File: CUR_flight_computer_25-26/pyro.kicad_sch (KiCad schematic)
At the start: 22 parts, among them J10 TB0011-350-02GR, J11 TB0011-350-02GR, J8 TB0011-350-02GR, J9 TB0011-350-02GR, U12 BUK9K25-40RAX, U13 BUK9K25-40RAX

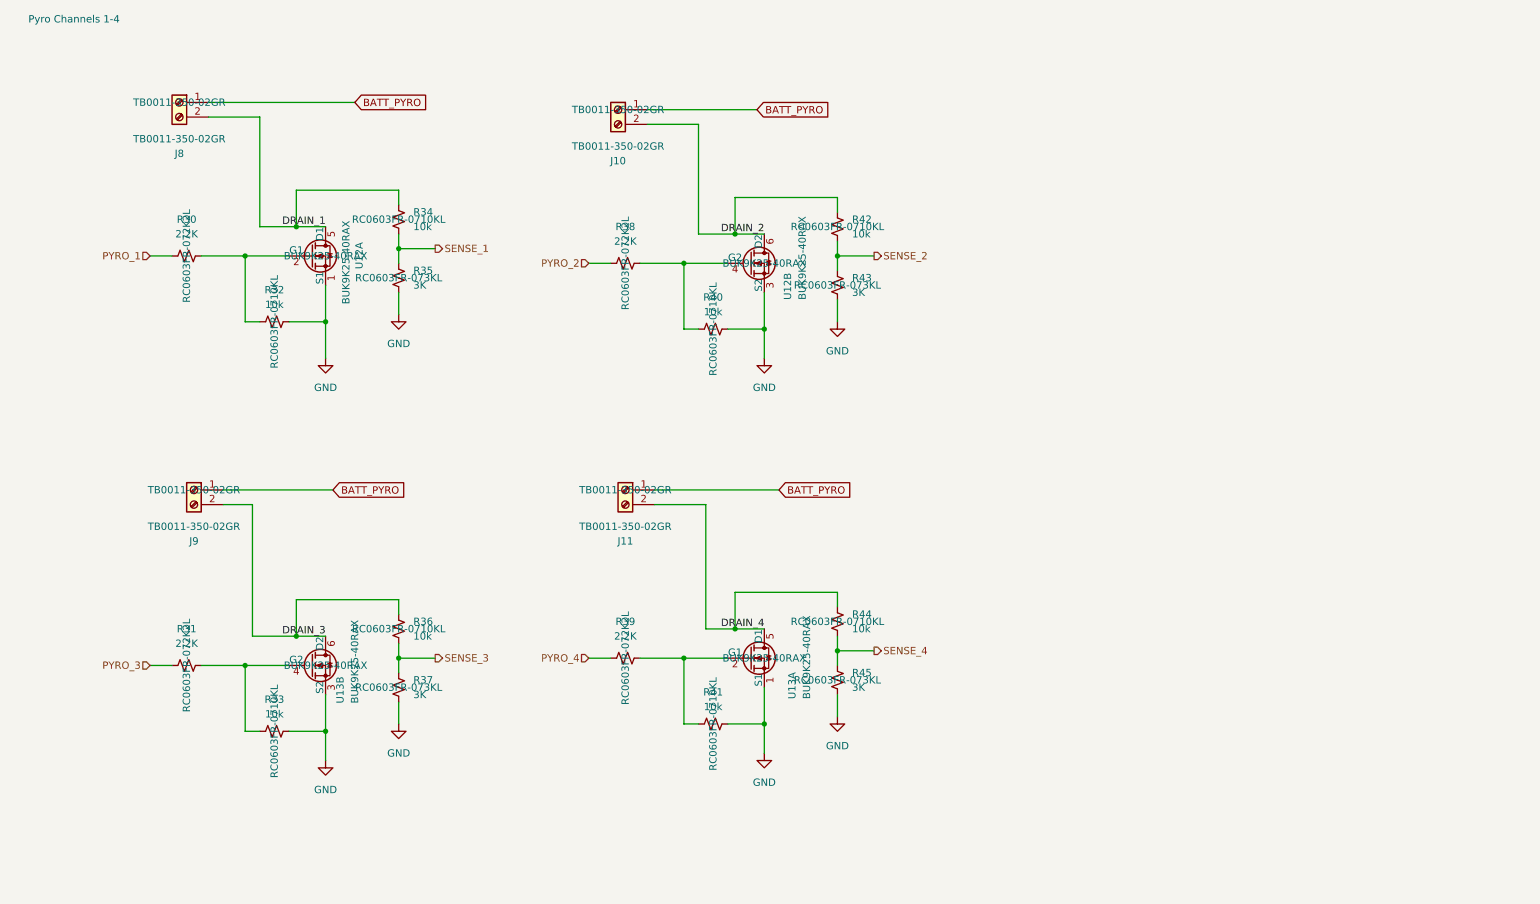
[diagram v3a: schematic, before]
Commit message: Hide MPNs
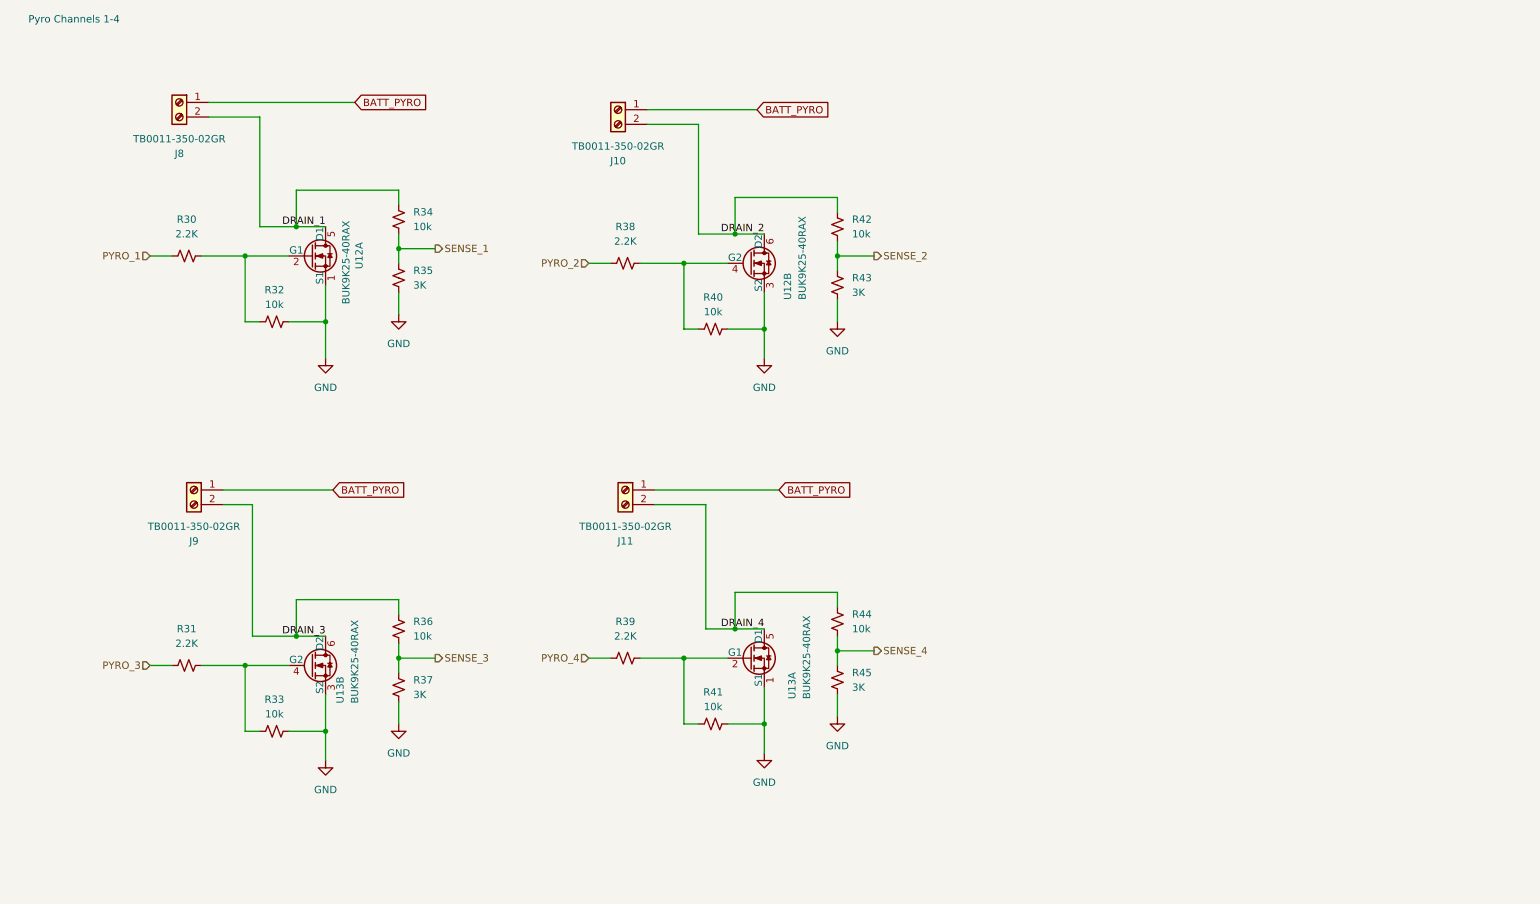
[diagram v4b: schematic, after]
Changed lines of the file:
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@@
 					(size 1.27 1.27)
 				)
+				(hide yes)
 			)
 		)
@@
 					(size 1.27 1.27)
 				)
+				(hide yes)
 			)
 		)
@@
 					(size 1.27 1.27)
 				)
+				(hide yes)
 			)
 		)
@@
 					(size 1.27 1.27)
 				)
+				(hide yes)
 			)
 		)
@@
 					(size 1.27 1.27)
 				)
+				(hide yes)
 			)
 		)
@@
 					(size 1.27 1.27)
 				)
+				(hide yes)
 			)
 		)
@@
 					(size 1.27 1.27)
 				)
+				(hide yes)
 			)
 		)
@@
 					(size 1.27 1.27)
 				)
+				(hide yes)
 			)
 		)
@@
 					(size 1.27 1.27)
 				)
+				(hide yes)
 			)
 		)
@@
 					(size 1.27 1.27)
 				)
+				(hide yes)
 			)
 		)
@@
 					(size 1.27 1.27)
 				)
+				(hide yes)
 			)
 		)
@@
 					(size 1.27 1.27)
 				)
+				(hide yes)
 			)
 		)
@@
 					(size 1.27 1.27)
 				)
+				(hide yes)
 			)
 		)
@@
 					(size 1.27 1.27)
 				)
+				(hide yes)
 			)
 		)
@@
 					(size 1.27 1.27)
 				)
+				(hide yes)
 			)
 		)
@@
 					(size 1.27 1.27)
 				)
+				(hide yes)
 			)
 		)
@@
 					(size 1.27 1.27)
 				)
+				(hide yes)
 			)
 		)
@@
 					(size 1.27 1.27)
 				)
+				(hide yes)
 			)
 		)
@@
 					(size 1.27 1.27)
 				)
+				(hide yes)
 			)
 		)
@@
 					(size 1.27 1.27)
 				)
+				(hide yes)
 			)
 		)
@@
 					(size 1.27 1.27)
 				)
+				(hide yes)
 			)
 		)
@@
 					(size 1.27 1.27)
 				)
+				(hide yes)
 			)
 		)
@@
 					(size 1.27 1.27)
 				)
+				(hide yes)
 			)
 		)
@@
 					(size 1.27 1.27)
 				)
-			)
-		)
+				(hide yes)
+			)
+		)

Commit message: Cleaned up schematic
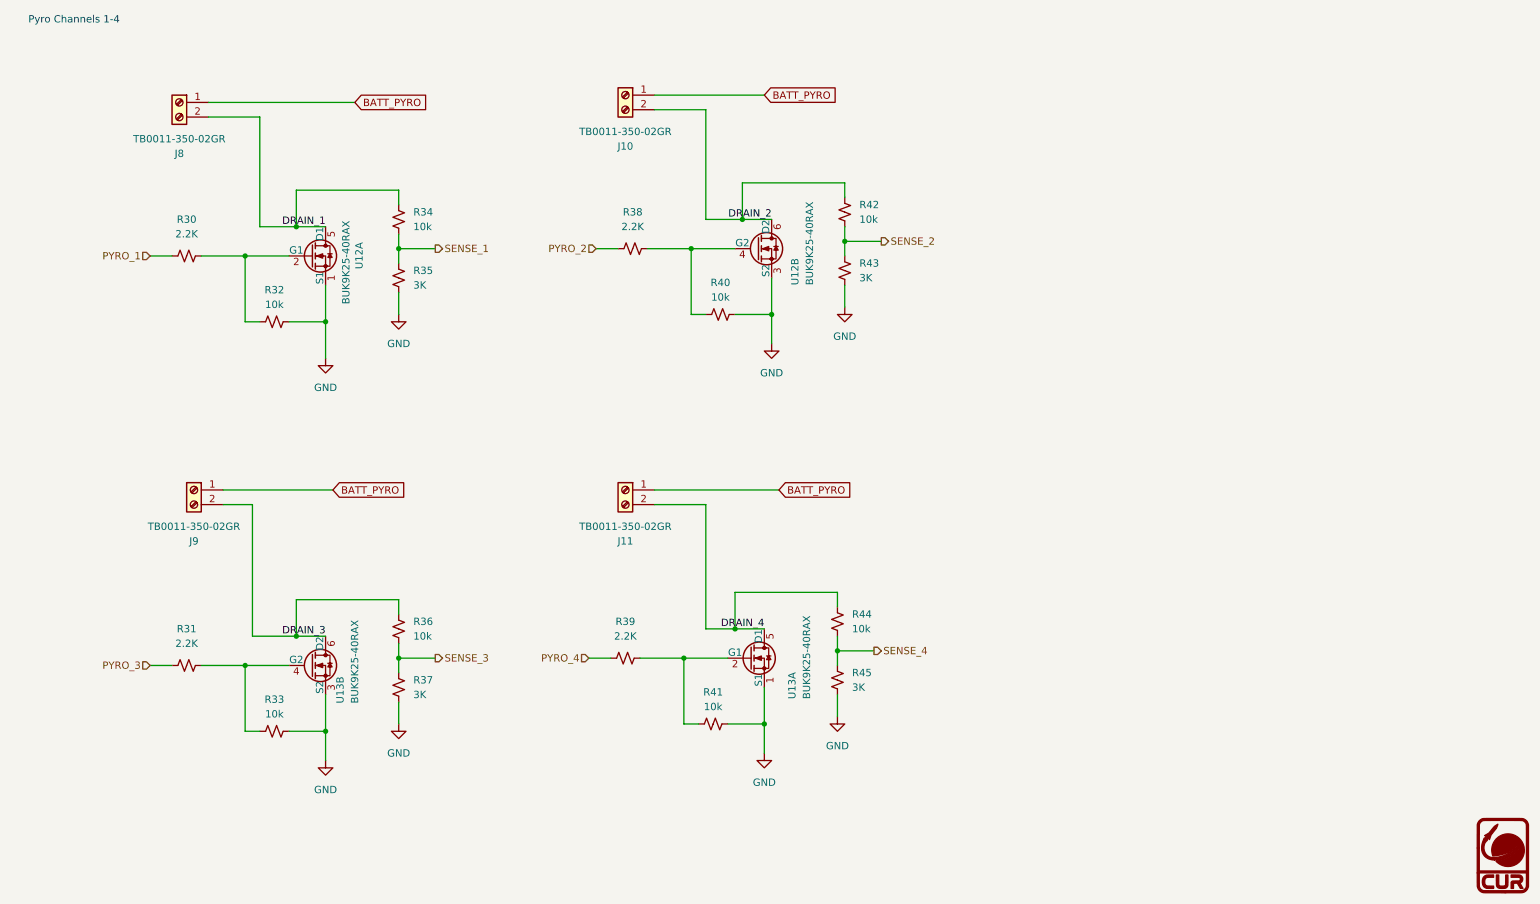
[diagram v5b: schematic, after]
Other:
- company: (none) -> Clarkson University Rocketry
- title: (none) -> Flight Computer
- moved on the sheet: J10, R38, R40, R42, R43, U12B

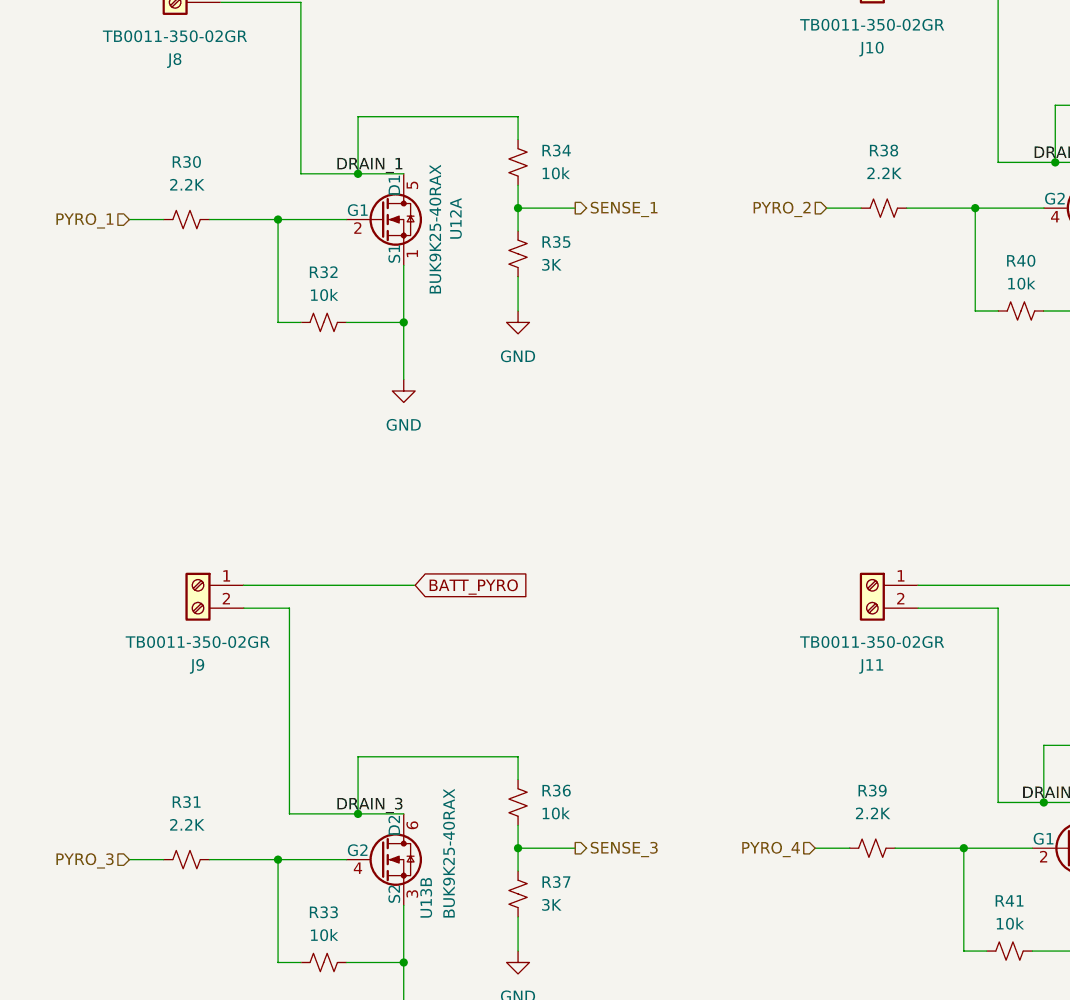
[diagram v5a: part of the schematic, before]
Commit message: BOM optimize resistors
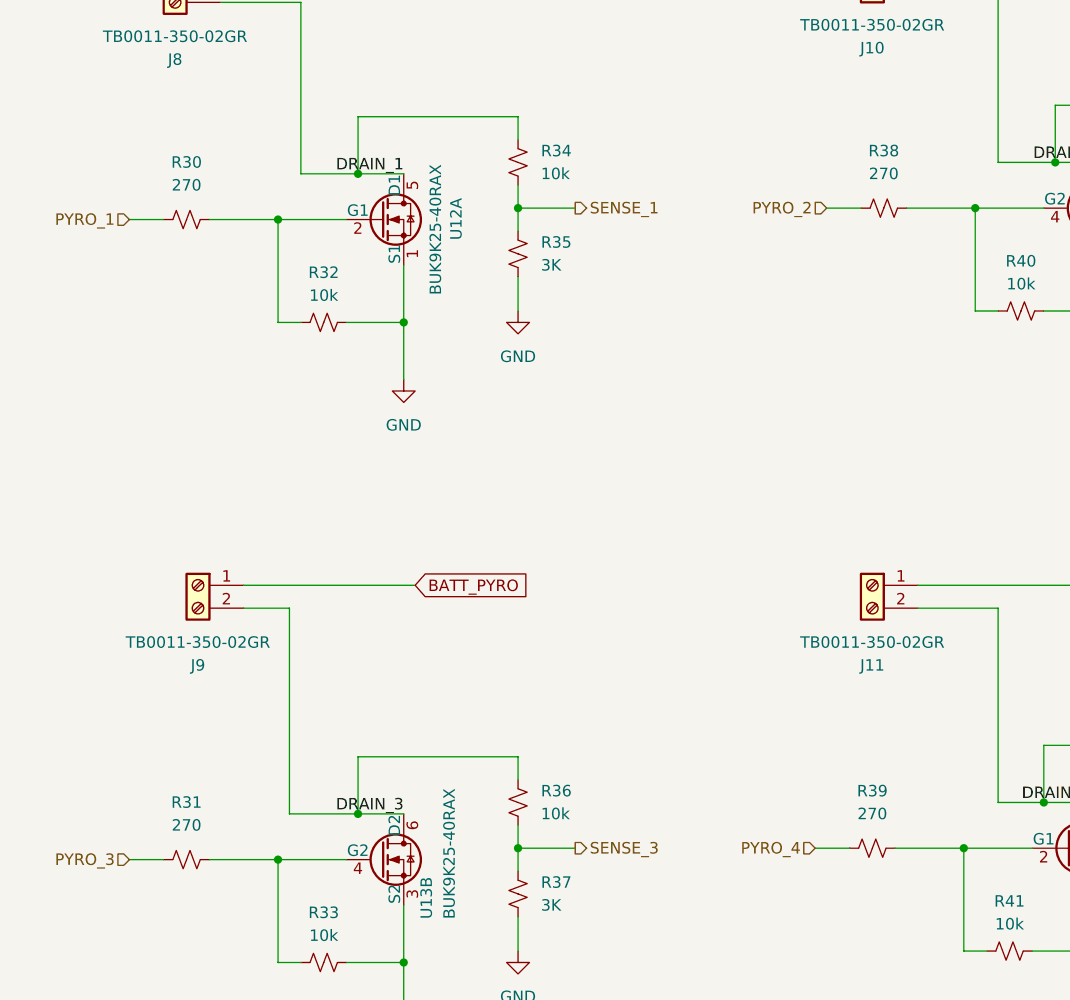
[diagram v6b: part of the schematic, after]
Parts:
- R30, R31, R38, R39: value 2.2K -> 270
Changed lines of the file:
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@@
 			)
 		)
-		(property "Value" "2.2K"
+		(property "Value" "270"
 			(at 127 135.89 90)
 			(effects
@@
 			)
 		)
-		(property "Value" "2.2K"
+		(property "Value" "270"
 			(at 50.8 66.04 90)
 			(effects
@@
 			)
 		)
-		(property "Value" "2.2K"
+		(property "Value" "270"
 			(at 128.27 64.77 90)
 			(effects
@@
 			)
 		)
-		(property "Value" "2.2K"
+		(property "Value" "270"
 			(at 50.8 137.16 90)
 			(effects

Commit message: Apply resistor MPNs
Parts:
- R30, R31, R38, R39: MPN RC0603FR-072K2L -> RC0603JR-07270RL
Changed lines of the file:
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@@
 			)
 		)
-		(property "MPN" "RC0603FR-072K2L"
+		(property "MPN" "RC0603JR-07270RL"
 			(at 127 139.7 0)
 			(effects
@@
 			)
 		)
-		(property "MPN" "RC0603FR-072K2L"
+		(property "MPN" "RC0603JR-07270RL"
 			(at 50.8 69.85 0)
 			(effects
@@
 			)
 		)
-		(property "MPN" "RC0603FR-072K2L"
+		(property "MPN" "RC0603JR-07270RL"
 			(at 128.27 68.58 0)
 			(effects
@@
 			)
 		)
-		(property "MPN" "RC0603FR-072K2L"
+		(property "MPN" "RC0603JR-07270RL"
 			(at 50.8 140.97 0)
 			(effects

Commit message: Final BOM and gerbers
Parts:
- R35, R37, R43, R45: value 3K -> 3k
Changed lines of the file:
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@@
 			)
 		)
-		(property "Value" "3K"
+		(property "Value" "3k"
 			(at 90.17 146.0499 0)
 			(effects
@@
 			)
 		)
-		(property "Value" "3K"
+		(property "Value" "3k"
 			(at 167.64 73.6599 0)
 			(effects
@@
 			)
 		)
-		(property "Value" "3K"
+		(property "Value" "3k"
 			(at 166.37 144.7799 0)
 			(effects
@@
 			)
 		)
-		(property "Value" "3K"
+		(property "Value" "3k"
 			(at 90.17 74.9299 0)
 			(effects
